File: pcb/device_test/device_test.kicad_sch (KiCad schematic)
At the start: 7 parts, among them J101 Conn_01x05, J102 Screw_Terminal_01x02, J103 Conn_01x05, J104 USB_A, J105 USB_OTG, J106 Conn_01x06, J107 Conn_01x07

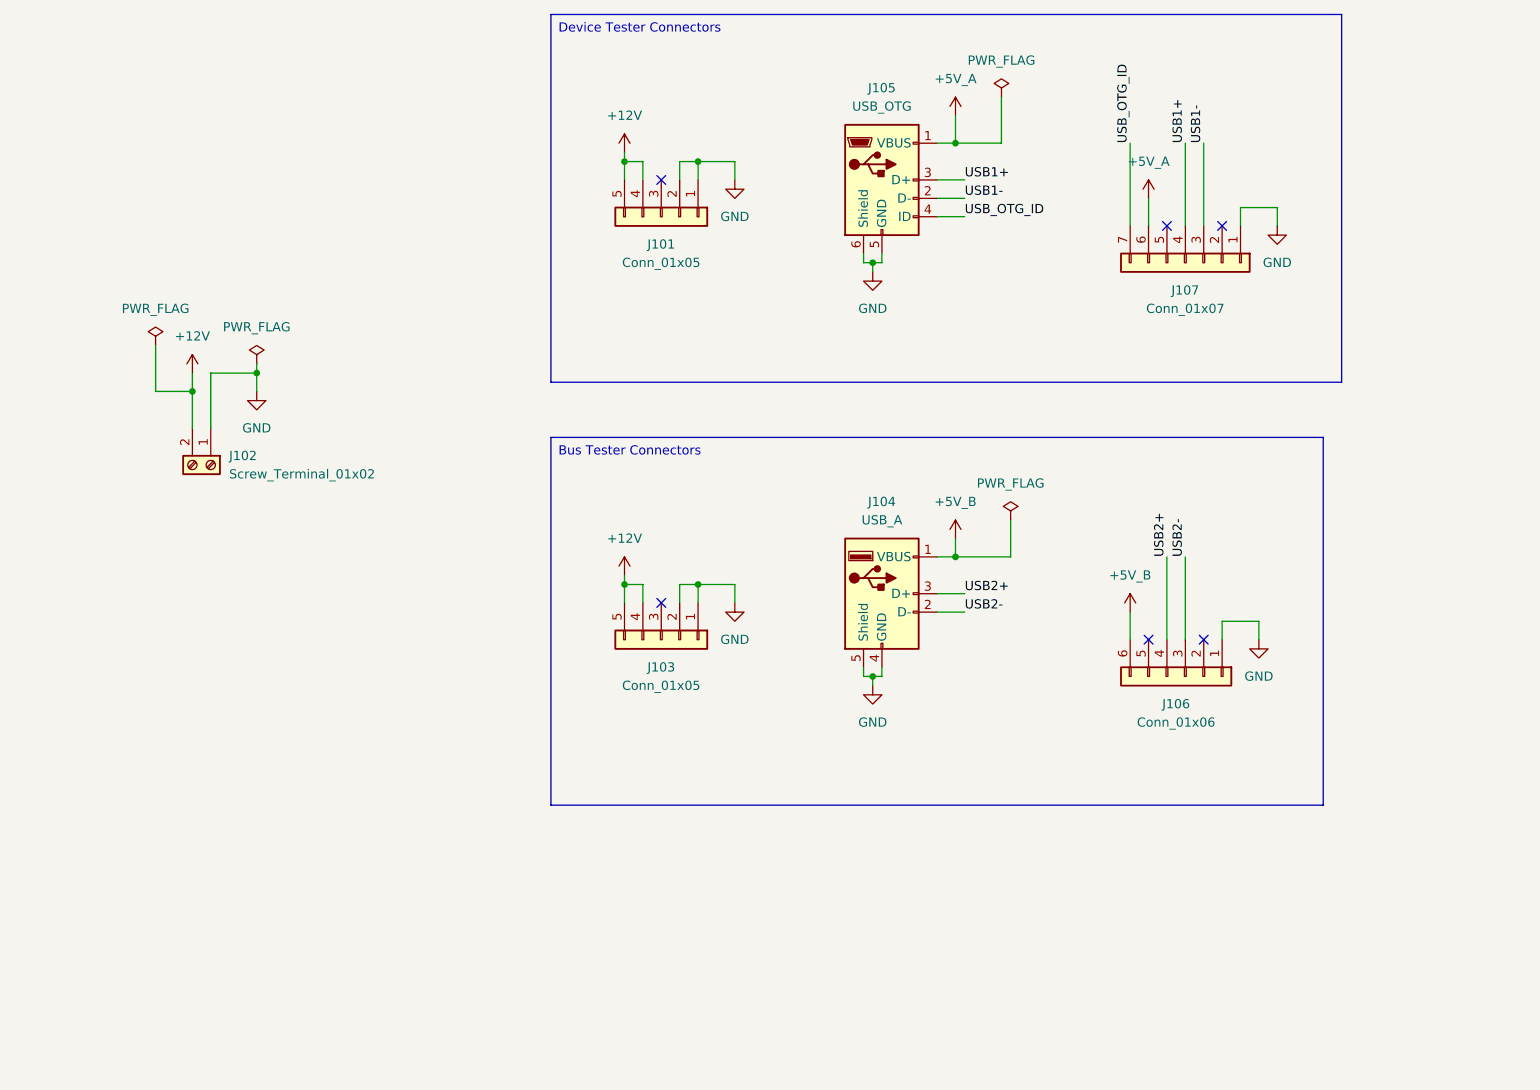
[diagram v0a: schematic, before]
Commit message: add leds to device tester
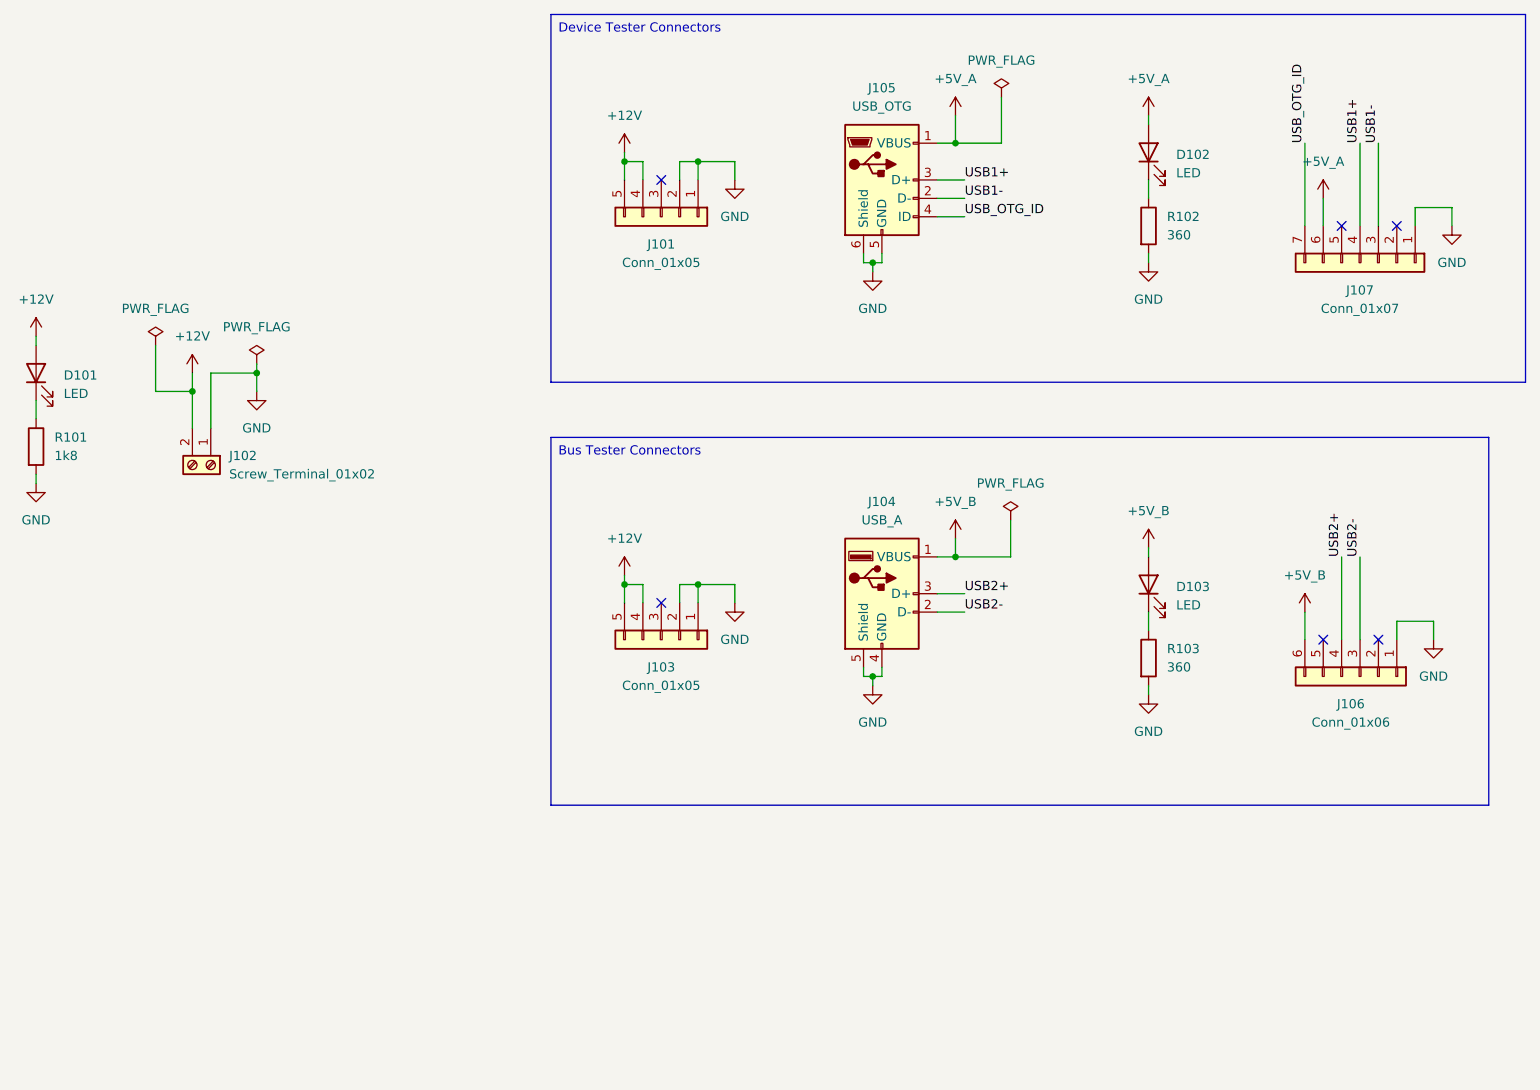
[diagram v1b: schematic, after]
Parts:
- added D101, D102, D103: LED, symbol Device:LED
- added R101: 1k8, symbol Device:R
- added R102, R103: 360, symbol Device:R
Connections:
- net +12V: now also D101.2 (A)
- net +5V_A: now also D102.2 (A)
- net +5V_B: now also D103.2 (A)
- net GND: now also R101.2, R102.2, R103.2
- new net: D102.1 (K), R102.1
- new net: D103.1 (K), R103.1
- new net: D101.1 (K), R101.1
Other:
- moved on the sheet: J106, J107

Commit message: update annotate
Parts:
- renumbered J102 to J101, J101 to J102, J105 to J104, J104 to J105, J107 to J106, J106 to J107
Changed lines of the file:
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@@
 		(dnp no)
 		(fields_autoplaced yes)
-		(property "Reference" "#PWR0112"
+		(property "Reference" "#PWR0119"
 			(at 242.57 129.54 0)
 			(effects
@@
 			(project "device_test"
 				(path "/5d20b266-567e-45c6-9e3e-145c2aea1daa"
-					(reference "#PWR0112")
+					(reference "#PWR0119")
 					(unit 1)
 				)
@@
 		(dnp no)
 		(fields_autoplaced yes)
-		(property "Reference" "#PWR0105"
+		(property "Reference" "#PWR0104"
 			(at 80.01 95.25 0)
 			(effects
@@
 			(project "device_test"
 				(path "/5d20b266-567e-45c6-9e3e-145c2aea1daa"
-					(reference "#PWR0105")
+					(reference "#PWR0104")
 					(unit 1)
 				)
@@
 		(dnp no)
 		(fields_autoplaced yes)
-		(property "Reference" "J105"
+		(property "Reference" "J104"
 			(at 166.37 46.99 0)
 			(effects
@@
 			(project ""
 				(path "/5d20b266-567e-45c6-9e3e-145c2aea1daa"
-					(reference "J105")
+					(reference "J104")
 					(unit 1)
 				)
@@
 		(dnp no)
 		(fields_autoplaced yes)
-		(property "Reference" "#PWR0108"
+		(property "Reference" "#PWR0112"
 			(at 176.53 113.03 0)
 			(effects
@@
 			(project "device_test"
 				(path "/5d20b266-567e-45c6-9e3e-145c2aea1daa"
-					(reference "#PWR0108")
+					(reference "#PWR0112")
 					(unit 1)
 				)
@@
 		(dnp no)
 		(fields_autoplaced yes)
-		(property "Reference" "J106"
+		(property "Reference" "J107"
 			(at 231.14 132.08 90)
 			(effects
@@
 			(project ""
 				(path "/5d20b266-567e-45c6-9e3e-145c2aea1daa"
-					(reference "J106")
+					(reference "J107")
 					(unit 1)
 				)
@@
 		(dnp no)
 		(fields_autoplaced yes)
-		(property "Reference" "#PWR0115"
+		(property "Reference" "#PWR0102"
 			(at 49.53 107.95 0)
 			(effects
@@
 			(project "device_test"
 				(path "/5d20b266-567e-45c6-9e3e-145c2aea1daa"
-					(reference "#PWR0115")
+					(reference "#PWR0102")
 					(unit 1)
 				)
@@
 		(dnp no)
 		(fields_autoplaced yes)
-		(property "Reference" "#PWR0106"
+		(property "Reference" "#PWR0108"
 			(at 146.05 124.46 0)
 			(effects
@@
 			(project "device_test"
 				(path "/5d20b266-567e-45c6-9e3e-145c2aea1daa"
-					(reference "#PWR0106")
+					(reference "#PWR0108")
 					(unit 1)
 				)
@@
 		(dnp no)
 		(fields_autoplaced yes)
-		(property "Reference" "#PWR0113"
+		(property "Reference" "#PWR0118"
 			(at 227.33 66.04 0)
 			(effects
@@
 			(project "device_test"
 				(path "/5d20b266-567e-45c6-9e3e-145c2aea1daa"
-					(reference "#PWR0113")
+					(reference "#PWR0118")
 					(unit 1)
 				)
@@
 		(dnp no)
 		(fields_autoplaced yes)
-		(property "Reference" "#PWR0119"
+		(property "Reference" "#PWR0115"
 			(at 203.2 114.3 0)
 			(effects
@@
 			)
 		)
-		(property "Description" "Power symbol creates a global label with name \"+12V\""
+		(property "Description" "Power symbol creates a global label with name \"+5V\""
 			(at 203.2 110.49 0)
 			(effects
@@
 			(project "device_test"
 				(path "/5d20b266-567e-45c6-9e3e-145c2aea1daa"
-					(reference "#PWR0119")
+					(reference "#PWR0115")
 					(unit 1)
 				)
@@
 		(dnp no)
 		(fields_autoplaced yes)
-		(property "Reference" "#PWR0116"
+		(property "Reference" "#PWR0101"
 			(at 49.53 85.09 0)
 			(effects
@@
 			(project "device_test"
 				(path "/5d20b266-567e-45c6-9e3e-145c2aea1daa"
-					(reference "#PWR0116")
+					(reference "#PWR0101")
 					(unit 1)
 				)
@@
 		(dnp no)
 		(fields_autoplaced yes)
-		(property "Reference" "J101"
+		(property "Reference" "J102"
 			(at 135.89 68.58 90)
 			(effects
@@
 			(project "device_test"
 				(path "/5d20b266-567e-45c6-9e3e-145c2aea1daa"
-					(reference "J101")
+					(reference "J102")
 					(unit 1)
 				)
@@
 		(dnp no)
 		(fields_autoplaced yes)
-		(property "Reference" "#PWR0118"
+		(property "Reference" "#PWR0114"
 			(at 203.2 77.47 0)
 			(effects
@@
 			(project "device_test"
 				(path "/5d20b266-567e-45c6-9e3e-145c2aea1daa"
-					(reference "#PWR0118")
+					(reference "#PWR0114")
 					(unit 1)
 				)
@@
 		(dnp no)
 		(fields_autoplaced yes)
-		(property "Reference" "J107"
+		(property "Reference" "J106"
 			(at 232.41 74.93 90)
 			(effects
@@
 			(project ""
 				(path "/5d20b266-567e-45c6-9e3e-145c2aea1daa"
-					(reference "J107")
+					(reference "J106")
 					(unit 1)
 				)
@@
 		(dnp no)
 		(fields_autoplaced yes)
-		(property "Reference" "J104"
+		(property "Reference" "J105"
 			(at 166.37 104.14 0)
 			(effects
@@
 			(project ""
 				(path "/5d20b266-567e-45c6-9e3e-145c2aea1daa"
-					(reference "J104")
+					(reference "J105")
 					(unit 1)
 				)
@@
 		(dnp no)
 		(fields_autoplaced yes)
-		(property "Reference" "#PWR0102"
+		(property "Reference" "#PWR0107"
 			(at 146.05 66.04 0)
 			(effects
@@
 			(project "device_test"
 				(path "/5d20b266-567e-45c6-9e3e-145c2aea1daa"
-					(reference "#PWR0102")
+					(reference "#PWR0107")
 					(unit 1)
 				)
@@
 		(dnp no)
 		(fields_autoplaced yes)
-		(property "Reference" "#PWR0101"
+		(property "Reference" "#PWR0105"
 			(at 130.81 59.69 0)
 			(effects
@@
 			(project "device_test"
 				(path "/5d20b266-567e-45c6-9e3e-145c2aea1daa"
-					(reference "#PWR0101")
+					(reference "#PWR0105")
 					(unit 1)
 				)
@@
 		(dnp no)
 		(fields_autoplaced yes)
-		(property "Reference" "#PWR0120"
+		(property "Reference" "#PWR0116"
 			(at 203.2 137.16 0)
 			(effects
@@
 			(project "device_test"
 				(path "/5d20b266-567e-45c6-9e3e-145c2aea1daa"
-					(reference "#PWR0120")
+					(reference "#PWR0116")
 					(unit 1)
 				)
@@
 		(dnp no)
 		(fields_autoplaced yes)
-		(property "Reference" "#PWR0114"
+		(property "Reference" "#PWR0120"
 			(at 245.11 72.39 0)
 			(effects
@@
 			(project "device_test"
 				(path "/5d20b266-567e-45c6-9e3e-145c2aea1daa"
-					(reference "#PWR0114")
+					(reference "#PWR0120")
 					(unit 1)
 				)
@@
 		(dnp no)
 		(fields_autoplaced yes)
-		(property "Reference" "#PWR0103"
+		(property "Reference" "#PWR0106"
 			(at 130.81 118.11 0)
 			(effects
@@
 			(project "device_test"
 				(path "/5d20b266-567e-45c6-9e3e-145c2aea1daa"
-					(reference "#PWR0103")
+					(reference "#PWR0106")
 					(unit 1)
 				)
@@
 		(dnp no)
 		(fields_autoplaced yes)
-		(property "Reference" "#PWR0117"
+		(property "Reference" "#PWR0113"
 			(at 203.2 54.61 0)
 			(effects
@@
 			)
 		)
-		(property "Description" "Power symbol creates a global label with name \"+12V\""
+		(property "Description" "Power symbol creates a global label with name \"+5V\""
 			(at 203.2 50.8 0)
 			(effects
@@
 			(project "device_test"
 				(path "/5d20b266-567e-45c6-9e3e-145c2aea1daa"
-					(reference "#PWR0117")
+					(reference "#PWR0113")
 					(unit 1)
 				)
@@
 		(dnp no)
 		(fields_autoplaced yes)
-		(property "Reference" "#PWR0111"
+		(property "Reference" "#PWR0117"
 			(at 224.79 123.19 0)
 			(effects
@@
 			(project "device_test"
 				(path "/5d20b266-567e-45c6-9e3e-145c2aea1daa"
-					(reference "#PWR0111")
+					(reference "#PWR0117")
 					(unit 1)
 				)
@@
 		(dnp no)
 		(fields_autoplaced yes)
-		(property "Reference" "J102"
+		(property "Reference" "J101"
 			(at 76.2 97.7899 90)
 			(effects
@@
 			(project ""
 				(path "/5d20b266-567e-45c6-9e3e-145c2aea1daa"
-					(reference "J102")
+					(reference "J101")
 					(unit 1)
 				)
@@
 		(dnp no)
 		(fields_autoplaced yes)
-		(property "Reference" "#PWR0107"
+		(property "Reference" "#PWR0110"
 			(at 165.1 135.89 0)
 			(effects
@@
 			(project "device_test"
 				(path "/5d20b266-567e-45c6-9e3e-145c2aea1daa"
-					(reference "#PWR0107")
+					(reference "#PWR0110")
 					(unit 1)
 				)
@@
 		(dnp no)
 		(fields_autoplaced yes)
-		(property "Reference" "#PWR0104"
+		(property "Reference" "#PWR0103"
 			(at 71.12 90.17 0)
 			(effects
@@
 			(project "device_test"
 				(path "/5d20b266-567e-45c6-9e3e-145c2aea1daa"
-					(reference "#PWR0104")
+					(reference "#PWR0103")
 					(unit 1)
 				)
@@
 		(dnp no)
 		(fields_autoplaced yes)
-		(property "Reference" "#PWR0110"
+		(property "Reference" "#PWR0111"
 			(at 176.53 54.61 0)
 			(effects
@@
 			(project "device_test"
 				(path "/5d20b266-567e-45c6-9e3e-145c2aea1daa"
-					(reference "#PWR0110")
-					(unit 1)
-				)
+					(reference "#PWR0111")
+					(unit 1)
+				)

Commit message: add footprints
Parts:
- D101, D102, D103: footprint (none) -> LED_SMD:LED_0805_2012Metric
- J102: footprint (none) -> Connector_PinSocket_2.54mm:PinSocket_1x05_P2.54mm_Horizontal
- J103: footprint (none) -> Connector_PinHeader_2.54mm:PinHeader_1x05_P2.54mm_Horizontal
- J104: footprint (none) -> USB:MicroUSB-920-E52A2021S10100; LCSC (none) -> C10418
- J105: footprint (none) -> USB:USB_A_C456020
- J106: footprint (none) -> Connector_PinSocket_2.54mm:PinSocket_1x07_P2.54mm_Horizontal
- J107: footprint (none) -> Connector_PinHeader_2.54mm:PinHeader_1x06_P2.54mm_Horizontal
- R101, R102, R103: footprint (none) -> Resistor_SMD:R_0805_2012Metric
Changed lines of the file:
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@@
 			)
 		)
-		(property "Footprint" ""
+		(property "Footprint" "USB:MicroUSB-920-E52A2021S10100"
 			(at 170.18 60.96 0)
 			(effects
@@
 			)
 		)
+		(property "LCSC" "C10418"
+			(at 166.37 59.69 0)
+			(effects
+				(font
+					(size 1.27 1.27)
+				)
+				(hide yes)
+			)
+		)
 		(pin "4"
 		)
@@
 			)
 		)
-		(property "Footprint" ""
+		(property "Footprint" "Connector_PinHeader_2.54mm:PinHeader_1x06_P2.54mm_Horizontal"
 			(at 232.41 128.27 0)
 			(effects
@@
 			)
 		)
+		(property "LCSC" ""
+			(at 232.41 128.27 0)
+			(effects
+				(font
+					(size 1.27 1.27)
+				)
+				(hide yes)
+			)
+		)
 		(pin "4"
 		)
@@
 			)
 		)
-		(property "Footprint" ""
+		(property "Footprint" "LED_SMD:LED_0805_2012Metric"
 			(at 203.2 55.88 0)
 			(effects
@@
 			)
 		)
-		(property "Footprint" ""
+		(property "Footprint" "LED_SMD:LED_0805_2012Metric"
 			(at 203.2 115.57 0)
 			(effects
@@
 			)
 		)
-		(property "Footprint" ""
+		(property "Footprint" "Connector_PinSocket_2.54mm:PinSocket_1x05_P2.54mm_Horizontal"
 			(at 135.89 64.77 0)
 			(effects
@@
 			)
 		)
+		(property "LCSC" ""
+			(at 135.89 64.77 0)
+			(effects
+				(font
+					(size 1.27 1.27)
+				)
+				(hide yes)
+			)
+		)
 		(pin "5"
 		)
@@
 			)
 		)
-		(property "Footprint" ""
+		(property "Footprint" "Connector_PinSocket_2.54mm:PinSocket_1x07_P2.54mm_Horizontal"
 			(at 232.41 71.12 0)
 			(effects
@@
 			)
 		)
+		(property "LCSC" ""
+			(at 232.41 71.12 0)
+			(effects
+				(font
+					(size 1.27 1.27)
+				)
+				(hide yes)
+			)
+		)
 		(pin "2"
 		)
@@
 			)
 		)
-		(property "Footprint" ""
+		(property "Footprint" "USB:USB_A_C456020"
 			(at 170.18 118.11 0)
 			(effects
@@
 			)
 		)
+		(property "LCSC" ""
+			(at 166.37 116.84 0)
+			(effects
+				(font
+					(size 1.27 1.27)
+				)
+				(hide yes)
+			)
+		)
 		(pin "2"
 		)
@@
 			)
 		)
-		(property "Footprint" ""
+		(property "Footprint" "Resistor_SMD:R_0805_2012Metric"
 			(at 201.422 66.04 90)
 			(effects
@@
 			)
 		)
-		(property "Footprint" ""
+		(property "Footprint" "Resistor_SMD:R_0805_2012Metric"
 			(at 201.422 125.73 90)
 			(effects
@@
 			)
 		)
-		(property "Footprint" ""
+		(property "Footprint" "Connector_PinHeader_2.54mm:PinHeader_1x05_P2.54mm_Horizontal"
 			(at 135.89 123.19 0)
 			(effects
@@
 			)
 		)
+		(property "LCSC" ""
+			(at 135.89 123.19 0)
+			(effects
+				(font
+					(size 1.27 1.27)
+				)
+				(hide yes)
+			)
+		)
 		(pin "5"
 		)
@@
 			)
 		)
-		(property "Footprint" ""
+		(property "Footprint" "LED_SMD:LED_0805_2012Metric"
 			(at 49.53 86.36 0)
 			(effects
@@
 			)
 		)
-		(property "Footprint" ""
+		(property "Footprint" "Resistor_SMD:R_0805_2012Metric"
 			(at 47.752 96.52 90)
 			(effects

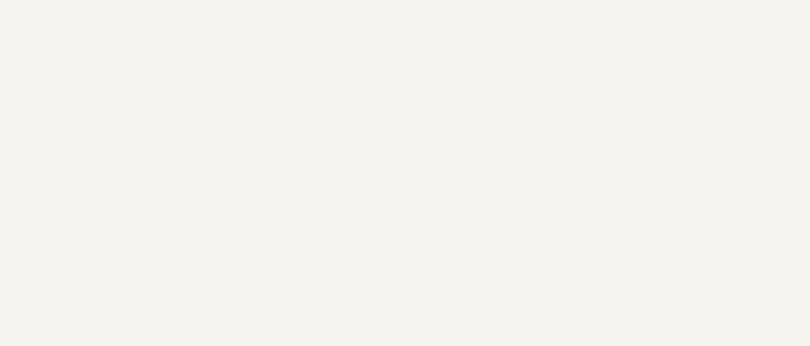
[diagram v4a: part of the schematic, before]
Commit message: add logo
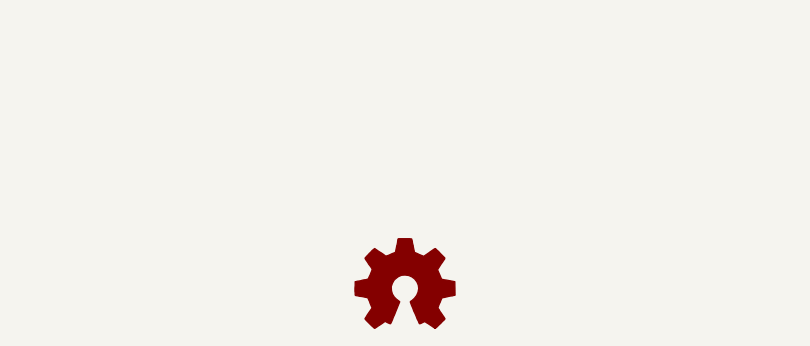
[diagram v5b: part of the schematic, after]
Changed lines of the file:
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@@
+	)
+	(symbol
+		(lib_id "Graphic:Logo_Open_Hardware_Small")
+		(at 153.67 179.07 0)
+		(unit 1)
+		(exclude_from_sim no)
+		(in_bom no)
+		(on_board yes)
+		(dnp no)
+		(fields_autoplaced yes)
+		(property "Reference" "#SYM101"
+			(at 153.67 172.085 0)
+			(effects
+				(font
+					(size 1.27 1.27)
+				)
+				(hide yes)
+			)
+		)
+		(property "Value" "Logo_Open_Hardware_Small"
+			(at 153.67 184.785 0)
+			(effects
+				(font
+					(size 1.27 1.27)
+				)
+				(hide yes)
+			)
+		)
+		(property "Footprint" "Symbol:OSHW-Logo_7.5x8mm_SilkScreen"
+			(at 153.67 179.07 0)
+			(effects
+				(font
+					(size 1.27 1.27)
+				)
+				(hide yes)
+			)
+		)
+		(property "Datasheet" "~"
+			(at 153.67 179.07 0)
+			(effects
+				(font
+					(size 1.27 1.27)
+				)
+				(hide yes)
+			)
+		)
+		(property "Description" "Open Hardware logo, small"
+			(at 153.67 179.07 0)
+			(effects
+				(font
+					(size 1.27 1.27)
+				)
+				(hide yes)
+			)
+		)
+		(property "Sim.Enable" "0"
+			(at 153.67 179.07 0)
+			(effects
+				(font
+					(size 1.27 1.27)
+				)
+				(hide yes)
+			)
+		)
+		(property "LCSC" ""
+			(at 153.67 179.07 0)
+			(effects
+				(font
+					(size 1.27 1.27)
+				)
+				(hide yes)
+			)
+		)
+		(instances
+			(project ""
+				(path "/5d20b266-567e-45c6-9e3e-145c2aea1daa"
+					(reference "#SYM101")
+					(unit 1)
+				)
+			)
+		)
 	)
 	(symbol
